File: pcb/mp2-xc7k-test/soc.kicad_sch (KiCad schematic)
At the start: 65 parts, among them J10 SMPM, J11 CONN_01X02, J8 CONN_01X03, J9 CONN_01X03, U15 AT24MAC402, U16 SIT9121AI-2BF-XXS200.000000G, U17 W25Q80BV, U18 S27KL0642GABHB020, U5 STM32MP257FAI3

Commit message: Continued layout, 454 unrouted
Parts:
- removed J11: CONN_01X02, symbol conn:CONN_01X02
- removed J8, J9: CONN_01X03, symbol conn:CONN_01X03
- added J12: PMOD_HOST, azonenberg_pcb:CONN_HEADER_2.54MM_2x6_RA_PMOD_HOST, symbol special-azonenberg:PMOD_HOST
- added J8: CONN_01X06, azonenberg_pcb:CONN_HEADER_2.54MM_1x6_REFLOW, symbol conn:CONN_01X06
- C136: footprint (none) -> azonenberg_pcb:EIA_0603_CAP_NOSILK
- D10, D11, D12, D4, D5, D6, D7, D8, D9: footprint azonenberg_pcb:EIA_0603_LED -> azonenberg_pcb:EIA_0402_LED
- J10: footprint (none) -> azonenberg_pcb:CONN_SMPM_AMPHENOL_C925-197J-51PT
- R60, R61, R62, R63, R64, R65, R66, R67, R68, R69, R70, R71, R72, R73, R74, R75, R76, R77, R82, R83, R84, R86, R87, R88, R89, R90, R91: footprint (none) -> azonenberg_pcb:EIA_0402_RES_NOSILK
- U17: footprint (none) -> azonenberg_pcb:SOIC_8_5.3MM
- U18: footprint (none) -> azonenberg_pcb:BGA_24_6x8_DEPOP1_1MM
- U5: footprint (none) -> azonenberg_pcb:BGA_436_18x18_DEPOP_0.8MM
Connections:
- net 3V3: now also J12.12 (3V3), J12.6 (3V3)
- net BOOTFAIL_N: now also J8.1 (P1)
- net GND: now also J12.11 (GND), J12.5 (GND), J8.6 (P6)
- net HYPERRAM_RST_N: now also U5.G5 (PI0); no longer U5.B20 (PB12)
- net PCIE_REF_AC_N: now also U16.4 (OUT_P); no longer U16.5 (OUT_N)
- net PCIE_REF_AC_P: now also U16.5 (OUT_N); no longer U16.4 (OUT_P)
- net SFP_MOD_ABS: now also U5.AA8 (PF8); no longer U5.T10 (PA15)
- net SFP_RX_LOS: now also U5.AB7 (PC11); no longer U5.U13 (PA10)
- net SFP_TX_DISABLE: now also U5.AB3 (PJ2); no longer U5.Y12 (PA13)
- net SFP_TX_FAULT: now also U5.AB8 (PF6); no longer U5.U10 (PA14)
- net SOC_LED0: now also U5.G4 (PG14); no longer U5.V12 (PF0)
- net SOC_LED1: now also U5.G3 (PG9); no longer U5.W11 (PF1)
- net SOC_LED2: now also U5.G2 (PI13); no longer U5.V10 (PF2)
- net SOC_LED3: now also U5.G1 (PI12); no longer U5.W10 (PF3)
- net SOC_LPUART_RX: now also R87.1; no longer R86.1
- net SOC_LPUART_TX: now also R86.1; no longer R87.1
- net SOC_LP_LED1: now also U5.P2 (PZ7); no longer U5.N4 (PZ3)
- net SOC_LP_LED2: now also U5.N3 (PZ9); no longer U5.R5 (PZ4)
- net SOC_LP_LED3: now also U5.N4 (PZ3); no longer U5.P5 (PZ5)
- net SOC_READY: now also U5.AA4 (PG4); no longer U5.W12 (PA11)
- net SOC_UART_RX: now also J8.5 (P5)
- net SOC_UART_TX: now also J8.4 (P4)
- net SOC_PMOD_DQ0: now reaches U5.AA12 (PC0)
- net SOC_PMOD_DQ0: now also J12.1 (D0)
- net SOC_PMOD_DQ3: now reaches U5.Y11 (PC2)
- net SOC_PMOD_DQ3: now also J12.4 (D3)
- net at R86.2: now also J8.3 (P3)
- net at R87.2: now also J8.2 (P2)
- net SOC_PMOD_DQ1: now reaches U5.AA11 (PH12)
- net SOC_PMOD_DQ1: now also J12.2 (D1)
- net SOC_PMOD_DQ6: now reaches U5.AA14 (PH6)
- net SOC_PMOD_DQ6: now also J12.9 (D6)
- net SOC_PMOD_DQ5: now reaches U5.AB11 (PH13)
- net SOC_PMOD_DQ5: now also J12.8 (D5)
- net SOC_PMOD_DQ4: now reaches U5.AB12 (PH9)
- net SOC_PMOD_DQ4: now also J12.7 (D4)
- net SOC_PMOD_DQ2: now reaches U5.Y14 (PA7)
- net SOC_PMOD_DQ2: now also J12.3 (D2)
- new net SOC_PMOD_DQ7: J12.10 (D7), U5.Y12 (PA13)
- no-connect marks 125 -> 117
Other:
- note added: "Debug PMOD"
- moved on the sheet: C133, C134, R86, R87

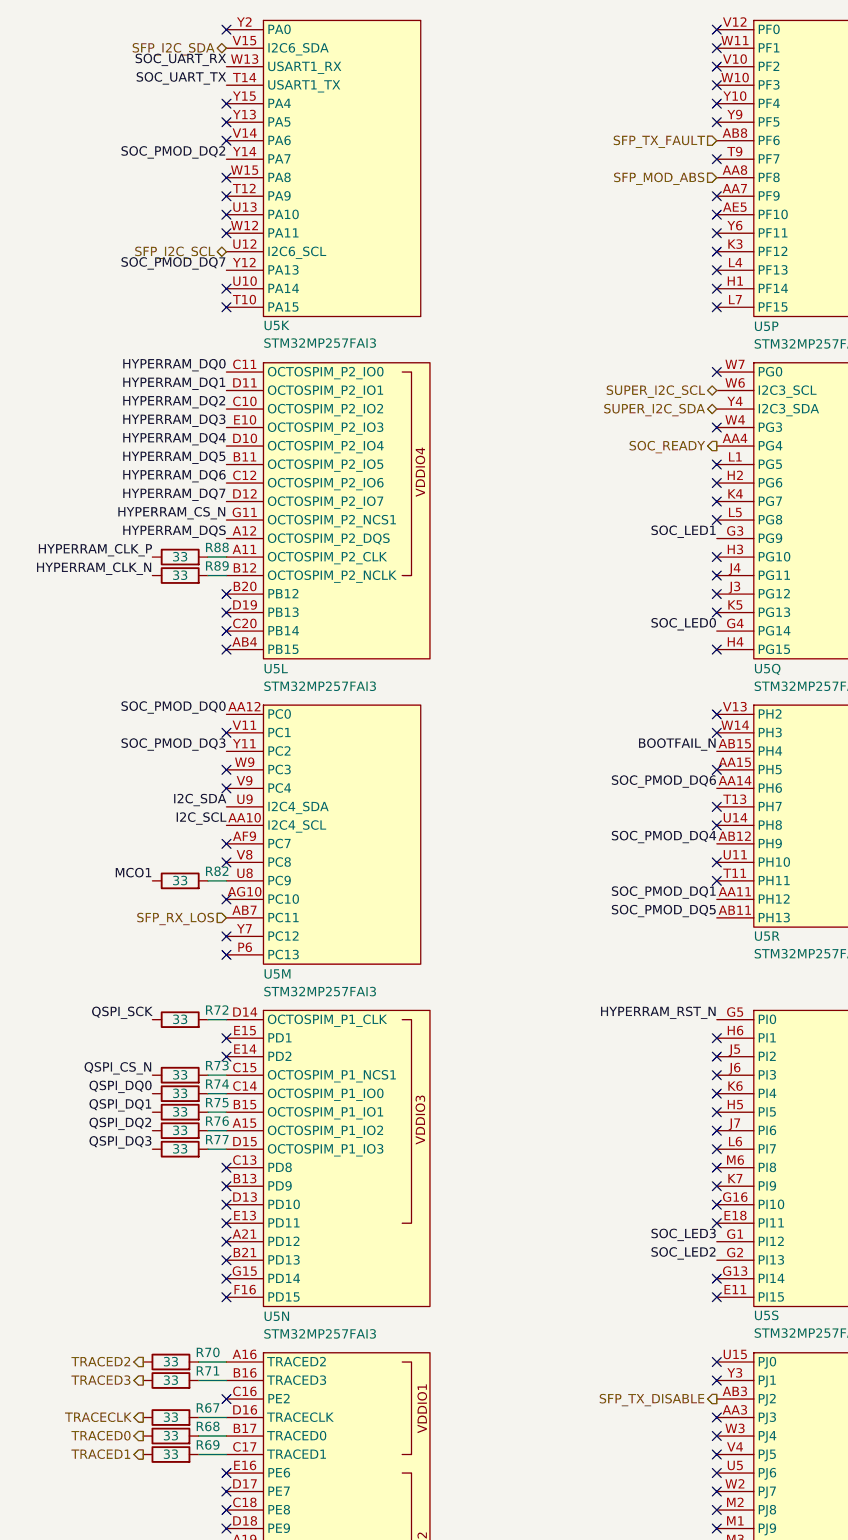
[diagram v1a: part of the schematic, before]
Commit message: Continued PCB routing, 344 nets left
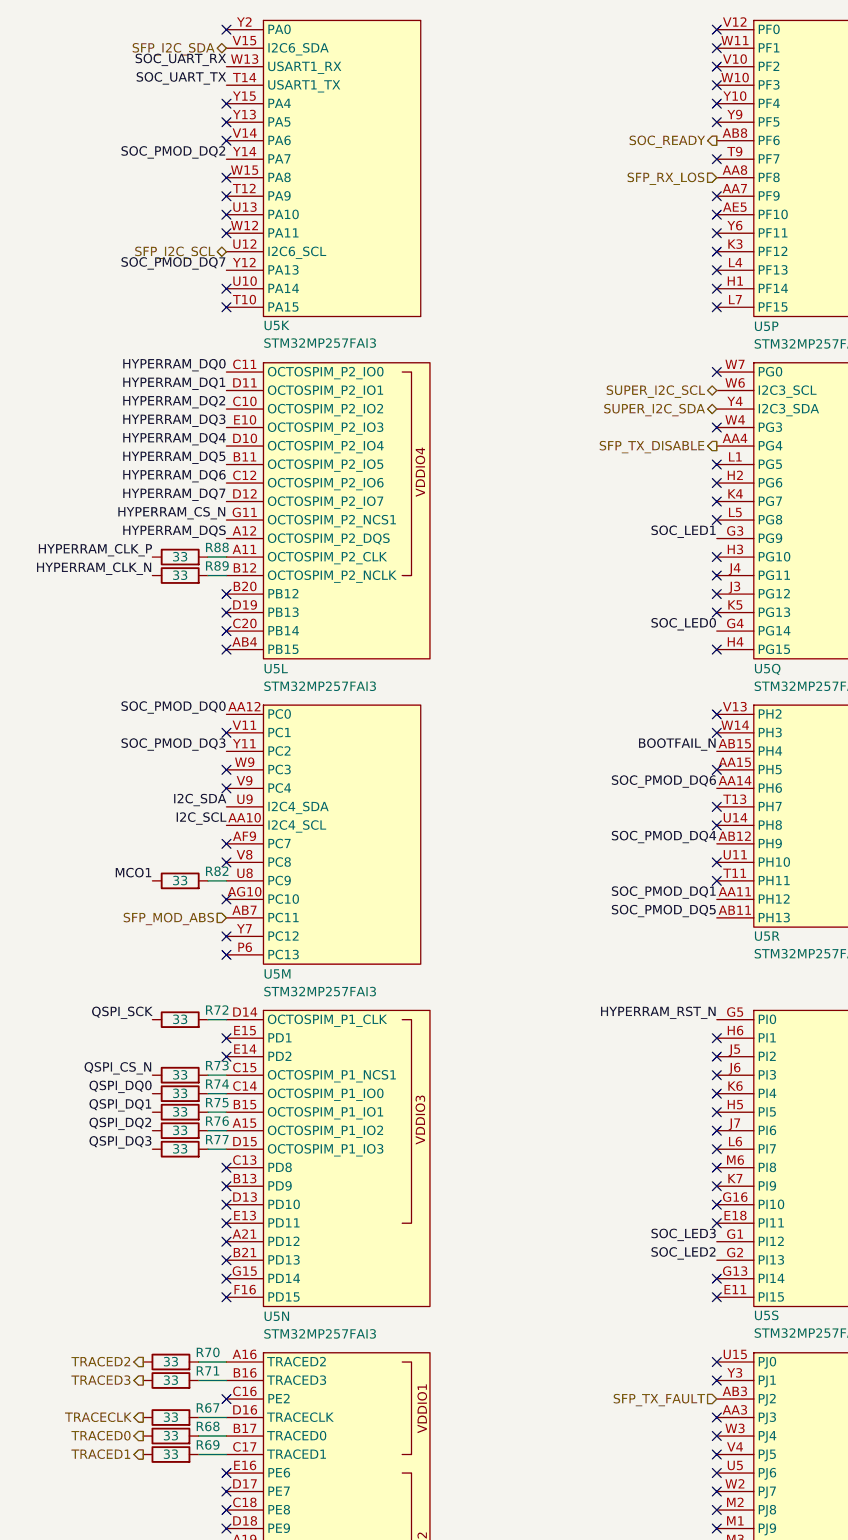
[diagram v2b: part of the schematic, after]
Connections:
- net SFP_MOD_ABS: now also U5.AB7 (PC11); no longer U5.AA8 (PF8)
- net SFP_RX_LOS: now also U5.AA8 (PF8); no longer U5.AB7 (PC11)
- net SFP_TX_DISABLE: now also U5.AA4 (PG4); no longer U5.AB3 (PJ2)
- net SFP_TX_FAULT: now also U5.AB3 (PJ2); no longer U5.AB8 (PF6)
- net SOC_READY: now also U5.AB8 (PF6); no longer U5.AA4 (PG4)
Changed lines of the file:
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@@
 	(hierarchical_label "SFP_MOD_ABS"
 		(shape input)
+		(at 41.91 144.78 180)
+		(effects
+			(font
+				(size 1.27 1.27)
+			)
+			(justify right)
+		)
+	)
+	(hierarchical_label "PCIE_TX_P"
+		(shape output)
+		(at 160.02 144.78 180)
+		(effects
+			(font
+				(size 1.27 1.27)
+			)
+			(justify right)
+		)
+	)
+	(hierarchical_label "SUPER_I2C_SCL"
+		(shape bidirectional)
+		(at 109.22 72.39 180)
+		(effects
+			(font
+				(size 1.27 1.27)
+			)
+			(justify right)
+		)
+	)
+	(hierarchical_label "SFP_I2C_SDA"
+		(shape bidirectional)
+		(at 41.91 25.4 180)
+		(effects
+			(font
+				(size 1.27 1.27)
+			)
+			(justify right)
+		)
+	)
+	(hierarchical_label "SFP_RX_LOS"
+		(shape input)
 		(at 109.22 43.18 180)
 		(effects
@@
 		)
 	)
-	(hierarchical_label "PCIE_TX_P"
-		(shape output)
-		(at 160.02 144.78 180)
-		(effects
-			(font
-				(size 1.27 1.27)
-			)
-			(justify right)
-		)
-	)
-	(hierarchical_label "SUPER_I2C_SCL"
-		(shape bidirectional)
-		(at 109.22 72.39 180)
-		(effects
-			(font
-				(size 1.27 1.27)
-			)
-			(justify right)
-		)
-	)
-	(hierarchical_label "SFP_I2C_SDA"
-		(shape bidirectional)
-		(at 41.91 25.4 180)
-		(effects
-			(font
-				(size 1.27 1.27)
-			)
-			(justify right)
-		)
-	)
-	(hierarchical_label "SFP_RX_LOS"
-		(shape input)
-		(at 41.91 144.78 180)
-		(effects
-			(font
-				(size 1.27 1.27)
-			)
-			(justify right)
-		)
-	)
 	(hierarchical_label "3V3"
 		(shape input)
@@
 	(hierarchical_label "SFP_TX_DISABLE"
 		(shape output)
+		(at 109.22 80.01 180)
+		(effects
+			(font
+				(size 1.27 1.27)
+			)
+			(justify right)
+		)
+	)
+	(hierarchical_label "GND"
+		(shape input)
+		(at 325.12 191.77 180)
+		(effects
+			(font
+				(size 1.27 1.27)
+			)
+			(justify right)
+		)
+	)
+	(hierarchical_label "PCIE_TX_N"
+		(shape output)
+		(at 160.02 147.32 180)
+		(effects
+			(font
+				(size 1.27 1.27)
+			)
+			(justify right)
+		)
+	)
+	(hierarchical_label "PCIE_RX_N"
+		(shape input)
+		(at 160.02 139.7 180)
+		(effects
+			(font
+				(size 1.27 1.27)
+			)
+			(justify right)
+		)
+	)
+	(hierarchical_label "SOC_READY"
+		(shape output)
+		(at 109.22 38.1 180)
+		(effects
+			(font
+				(size 1.27 1.27)
+			)
+			(justify right)
+		)
+	)
+	(hierarchical_label "PCIE_RX_P"
+		(shape input)
+		(at 160.02 137.16 180)
+		(effects
+			(font
+				(size 1.27 1.27)
+			)
+			(justify right)
+		)
+	)
+	(hierarchical_label "TRACECLK"
+		(shape output)
+		(at 30.48 213.36 180)
+		(effects
+			(font
+				(size 1.27 1.27)
+			)
+			(justify right)
+		)
+	)
+	(hierarchical_label "TRACED3"
+		(shape output)
+		(at 30.48 208.28 180)
+		(effects
+			(font
+				(size 1.27 1.27)
+			)
+			(justify right)
+		)
+	)
+	(hierarchical_label "SFP_I2C_SCL"
+		(shape bidirectional)
+		(at 41.91 53.34 180)
+		(effects
+			(font
+				(size 1.27 1.27)
+			)
+			(justify right)
+		)
+	)
+	(hierarchical_label "TRACED2"
+		(shape output)
+		(at 30.48 205.74 180)
+		(effects
+			(font
+				(size 1.27 1.27)
+			)
+			(justify right)
+		)
+	)
+	(hierarchical_label "PCIE_REF_N"
+		(shape output)
+		(at 160.02 127 180)
+		(effects
+			(font
+				(size 1.27 1.27)
+			)
+			(justify right)
+		)
+	)
+	(hierarchical_label "TRACED0"
+		(shape output)
+		(at 30.48 215.9 180)
+		(effects
+			(font
+				(size 1.27 1.27)
+			)
+			(justify right)
+		)
+	)
+	(hierarchical_label "SFP_TX_FAULT"
+		(shape input)
 		(at 109.22 210.82 180)
 		(effects
 			(font
-				(size 1.27 1.27)
-			)
-			(justify right)
-		)
-	)
-	(hierarchical_label "GND"
-		(shape input)
-		(at 325.12 191.77 180)
-		(effects
-			(font
-				(size 1.27 1.27)
-			)
-			(justify right)
-		)
-	)
-	(hierarchical_label "PCIE_TX_N"
-		(shape output)
-		(at 160.02 147.32 180)
-		(effects
-			(font
-				(size 1.27 1.27)
-			)
-			(justify right)
-		)
-	)
-	(hierarchical_label "PCIE_RX_N"
-		(shape input)
-		(at 160.02 139.7 180)
-		(effects
-			(font
-				(size 1.27 1.27)
-			)
-			(justify right)
-		)
-	)
-	(hierarchical_label "SOC_READY"
-		(shape output)
-		(at 109.22 80.01 180)
-		(effects
-			(font
-				(size 1.27 1.27)
-			)
-			(justify right)
-		)
-	)
-	(hierarchical_label "PCIE_RX_P"
-		(shape input)
-		(at 160.02 137.16 180)
-		(effects
-			(font
-				(size 1.27 1.27)
-			)
-			(justify right)
-		)
-	)
-	(hierarchical_label "TRACECLK"
-		(shape output)
-		(at 30.48 213.36 180)
-		(effects
-			(font
-				(size 1.27 1.27)
-			)
-			(justify right)
-		)
-	)
-	(hierarchical_label "TRACED3"
-		(shape output)
-		(at 30.48 208.28 180)
-		(effects
-			(font
-				(size 1.27 1.27)
-			)
-			(justify right)
-		)
-	)
-	(hierarchical_label "SFP_I2C_SCL"
-		(shape bidirectional)
-		(at 41.91 53.34 180)
-		(effects
-			(font
-				(size 1.27 1.27)
-			)
-			(justify right)
-		)
-	)
-	(hierarchical_label "TRACED2"
-		(shape output)
-		(at 30.48 205.74 180)
-		(effects
-			(font
-				(size 1.27 1.27)
-			)
-			(justify right)
-		)
-	)
-	(hierarchical_label "PCIE_REF_N"
-		(shape output)
-		(at 160.02 127 180)
-		(effects
-			(font
-				(size 1.27 1.27)
-			)
-			(justify right)
-		)
-	)
-	(hierarchical_label "TRACED0"
-		(shape output)
-		(at 30.48 215.9 180)
-		(effects
-			(font
-				(size 1.27 1.27)
-			)
-			(justify right)
-		)
-	)
-	(hierarchical_label "SFP_TX_FAULT"
-		(shape input)
-		(at 109.22 38.1 180)
-		(effects
-			(font

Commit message: Test board ready for design review
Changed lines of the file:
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@@
 	(paper "A3")
 	(title_block
-		(date "2025-12-19")
+		(date "2025-12-25")
 		(rev "0.1")
 	)
@@
 			)
 		)
-		(pin "AE5"
+		(pin "AA6"
 		)
 		(pin "U16"
@@
 		(pin "AA7"
 		)
-		(pin "AG10"
+		(pin "Y8"
 		)
 		(pin "L7"
@@
 		(pin "W9"
 		)
-		(pin "AF9"
+		(pin "T8"
 		)
 		(pin "T6"
@@
 			)
 		)
-		(pin "AE5"
+		(pin "T8"
 		)
 		(pin "U16"
@@
 		(pin "AA7"
 		)
-		(pin "AG10"
+		(pin "AA6"
 		)
 		(pin "L7"
@@
 		(pin "W9"
 		)
-		(pin "AF9"
+		(pin "Y8"
 		)
 		(pin "T6"
@@
 			)
 		)
-		(pin "AE5"
+		(pin "T8"
 		)
 		(pin "U16"
@@
 		(pin "AA7"
 		)
-		(pin "AG10"
+		(pin "Y8"
 		)
 		(pin "L7"
@@
 		(pin "W9"
 		)
-		(pin "AF9"
+		(pin "AA6"
 		)
 		(pin "T6"
@@
 			)
 		)
-		(pin "AE5"
+		(pin "T8"
 		)
 		(pin "U16"
@@
 		(pin "AA7"
 		)
-		(pin "AG10"
+		(pin "Y8"
 		)
 		(pin "L7"
@@
 		(pin "W9"
 		)
-		(pin "AF9"
+		(pin "AA6"
 		)
 		(pin "T6"
@@
 			)
 		)
-		(pin "AE5"
+		(pin "T8"
 		)
 		(pin "U16"
@@
 		(pin "AA7"
 		)
-		(pin "AG10"
+		(pin "AA6"
 		)
 		(pin "L7"
@@
 		(pin "W9"
 		)
-		(pin "AF9"
+		(pin "Y8"
 		)
 		(pin "T6"
@@
 			)
 		)
-		(pin "AE5"
+		(pin "AA6"
 		)
 		(pin "U16"
@@
 		(pin "AA7"
 		)
-		(pin "AG10"
+		(pin "Y8"
 		)
 		(pin "L7"
@@
 		(pin "W9"
 		)
-		(pin "AF9"
+		(pin "T8"
 		)
 		(pin "T6"
@@
 			)
 		)
-		(pin "AE5"
+		(pin "T8"
 		)
 		(pin "U16"
@@
 		(pin "AA7"
 		)
-		(pin "AG10"
+		(pin "Y8"
 		)
 		(pin "L7"
@@
 		(pin "W9"
 		)
-		(pin "AF9"
+		(pin "AA6"
 		)
 		(pin "T6"
@@
 			)
 		)
-		(pin "AE5"
+		(pin "AA6"
 		)
 		(pin "U16"
@@
 		(pin "AA7"
 		)
-		(pin "AG10"
+		(pin "T8"
 		)
 		(pin "L7"
@@
 		(pin "W9"
 		)
-		(pin "AF9"
+		(pin "Y8"
 		)
 		(pin "T6"
@@
 			)
 		)
-		(pin "AE5"
+		(pin "AA6"
 		)
 		(pin "U16"
@@
 		(pin "AA7"
 		)
-		(pin "AG10"
+		(pin "T8"
 		)
 		(pin "L7"
@@
 		(pin "W9"
 		)
-		(pin "AF9"
+		(pin "Y8"
 		)
 		(pin "T6"
@@
 			)
 		)
-		(pin "AE5"
+		(pin "T8"
 		)
 		(pin "U16"
@@
 		(pin "AA7"
 		)
-		(pin "AG10"
+		(pin "Y8"
 		)
 		(pin "L7"
@@
 		(pin "W9"
 		)
-		(pin "AF9"
+		(pin "AA6"
 		)
 		(pin "T6"
@@
 			)
 		)
-		(pin "AE5"
+		(pin "Y8"
 		)
 		(pin "U16"
@@
 		(pin "AA7"
 		)
-		(pin "AG10"
+		(pin "T8"
 		)
 		(pin "L7"
@@
 		(pin "W9"
 		)
-		(pin "AF9"
+		(pin "AA6"
 		)
 		(pin "T6"
@@
 			)
 		)
-		(pin "AE5"
+		(pin "Y8"
 		)
 		(pin "U16"
@@
 		(pin "AA7"
 		)
-		(pin "AG10"
+		(pin "T8"
 		)
 		(pin "L7"
@@
 		(pin "W9"
 		)
-		(pin "AF9"
+		(pin "AA6"
 		)
 		(pin "T6"
@@
 			)
 		)
-		(pin "AE5"
+		(pin "AA6"
 		)
 		(pin "U16"
@@
 		(pin "AA7"
 		)
-		(pin "AG10"
+		(pin "Y8"
 		)
 		(pin "L7"
@@
 		(pin "W9"
 		)
-		(pin "AF9"
+		(pin "T8"
 		)
 		(pin "T6"
